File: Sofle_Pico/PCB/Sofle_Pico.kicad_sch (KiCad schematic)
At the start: 81 parts, among them J1 Pimaroni Trackball, J2 4PIN, J3 OLED, J5 Conn_01x05_Socket, J6 Conn_01x05_Socket, Q1 TIP120, SW1 SW_PUSH_LED, SW10 SW_PUSH_LED, SW11 SW_PUSH_LED, SW12 SW_PUSH_LED, SW13 SW_PUSH_LED, SW14 SW_PUSH_LED, SW15 SW_PUSH_LED, SW16 SW_PUSH_LED, SW17 SW_PUSH_LED, SW18 SW_PUSH_LED, SW19 SW_PUSH_LED, SW2 SW_PUSH_LED, SW20 SW_PUSH_LED, SW21 SW_PUSH_LED, SW22 SW_PUSH_LED, SW23 SW_PUSH_LED, SW24 SW_PUSH_LED, SW25 Rotary_Encoder_Switch, SW26 SW_PUSH_LED, SW27 SW_PUSH_LED, SW28 SW_PUSH_LED, SW29 SW_PUSH_LED, SW3 SW_PUSH_LED, SW30 SW_PUSH_LED, SW4 SW_PUSH_LED, SW5 SW_PUSH_LED, SW6 SW_PUSH_LED, SW7 SW_PUSH_LED, SW8 SW_PUSH_LED, SW9 SW_PUSH_LED, U1 SN74AHCT1G125, U3 Pico

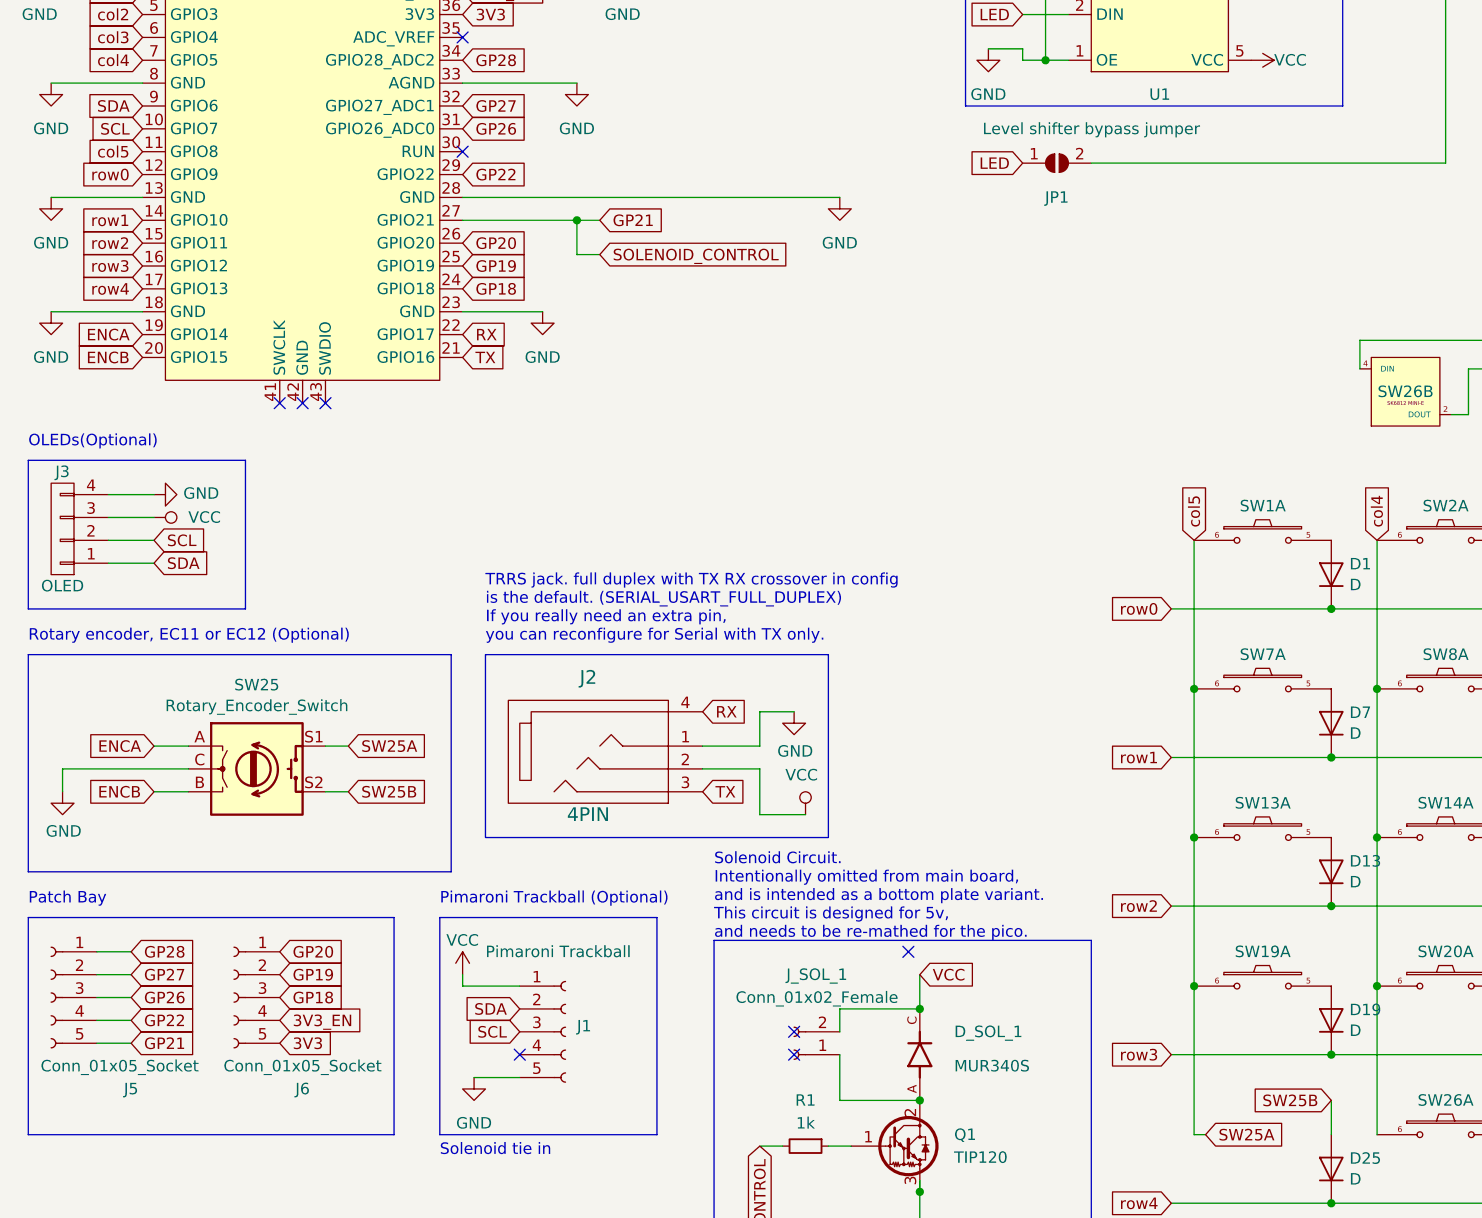
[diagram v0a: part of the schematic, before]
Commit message: Refactored LED to remove drill holes replaced drill holes with edge cuts minor trace revisions to decrease acid traps
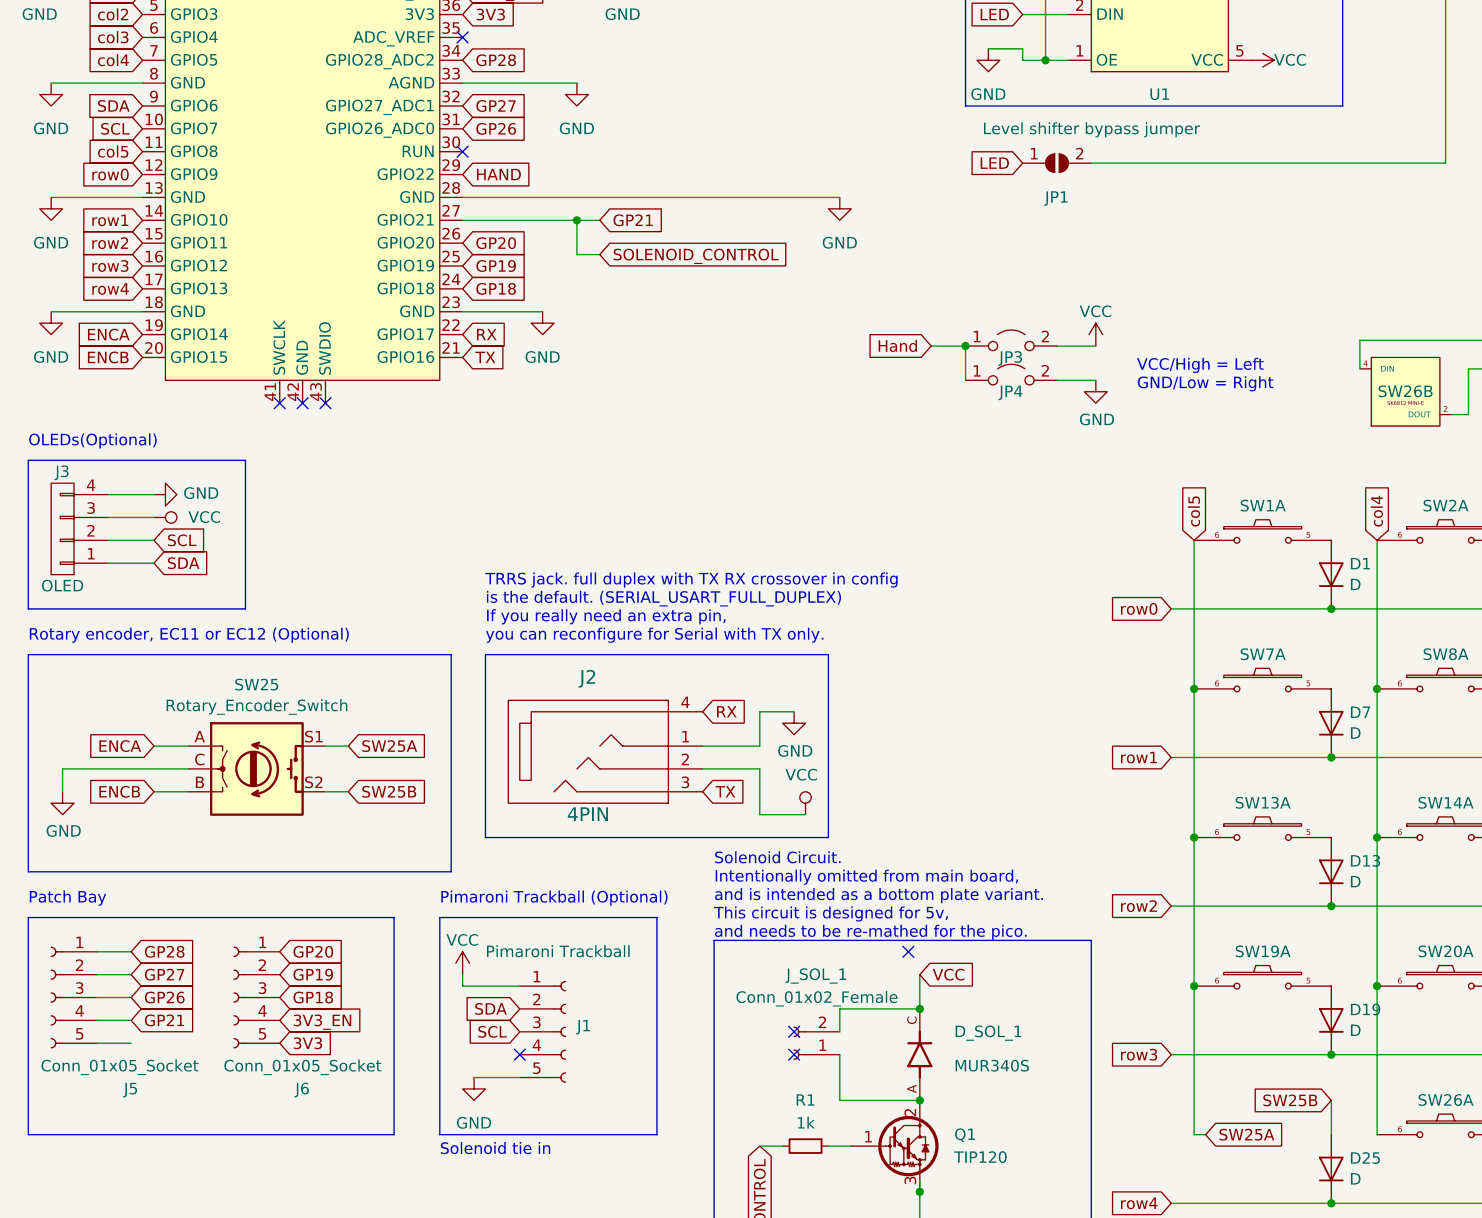
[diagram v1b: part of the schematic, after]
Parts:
- added JP3: LEFT, Keyboard Common:Jumper_Mini, symbol Jumper:Jumper_2_Open
- added JP4: RIGHT, Keyboard Common:Jumper_Mini, symbol Jumper:Jumper_2_Open
- SW1, SW10, SW11, SW12, SW13, SW14, SW15, SW16, SW17, SW18, SW19, SW2, SW20, SW21, SW22, SW23, SW24, SW26, SW27, SW28, SW29, SW3, SW30, SW4, SW5, SW6, SW7, SW8, SW9: footprint Sofle_Pico:Cherry_MX_DS_Hotswap_miniE_1U_v3.5 -> Sofle_Pico:Cherry_MX_DS_Hotswap_miniE_1U_v3.5.2
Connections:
- net GND: now also JP4.2 (B)
- net GP21: now also J5.4 (Pin_4); no longer J5.5 (Pin_5)
- net VCC: now also JP3.2 (B)
- net GP22 renamed HAND
- net HAND: no longer J5.4 (Pin_4)
- new net Hand: JP3.1 (A), JP4.1 (A)
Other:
- note added: "VCC/High = Left GND/Low = Right"

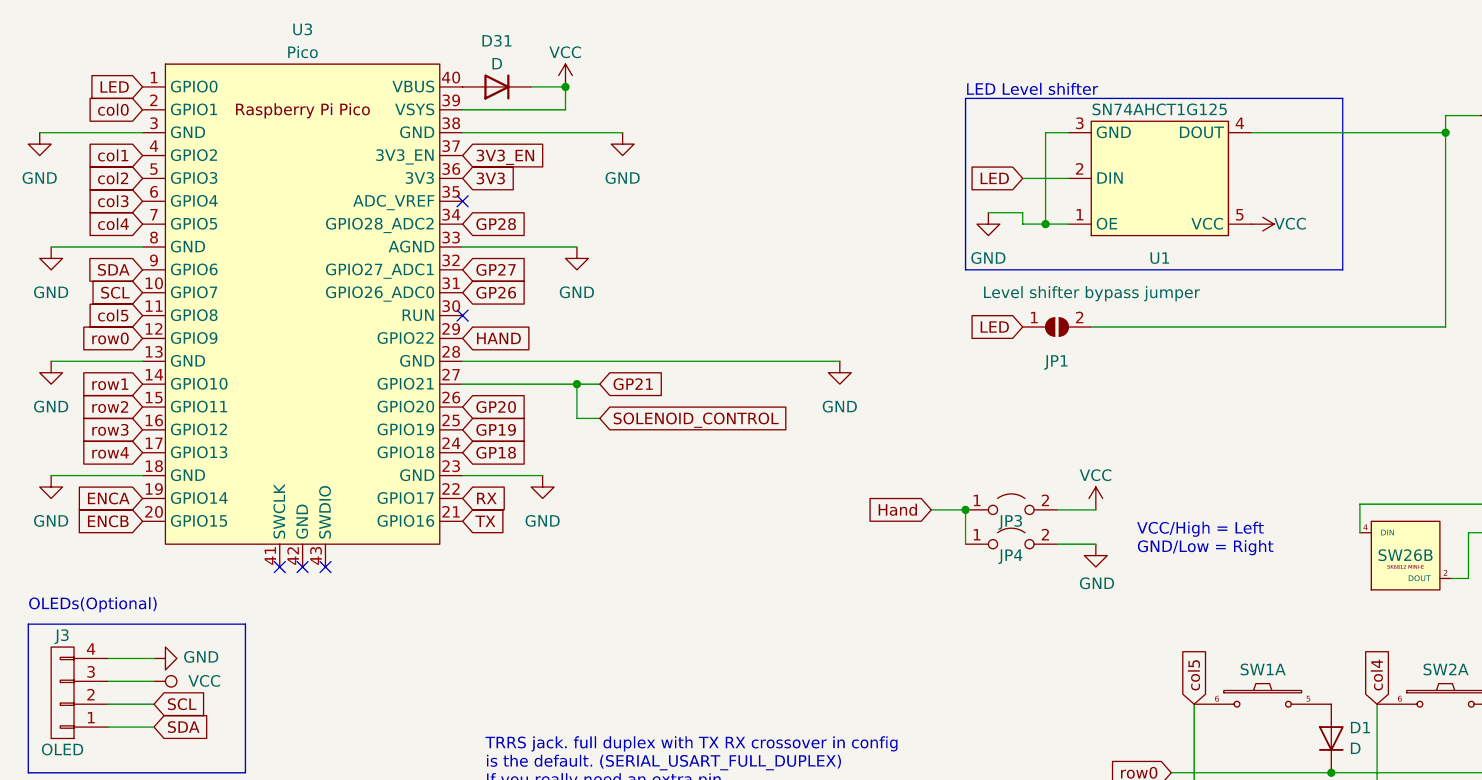
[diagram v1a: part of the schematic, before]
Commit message: Added handedness pin
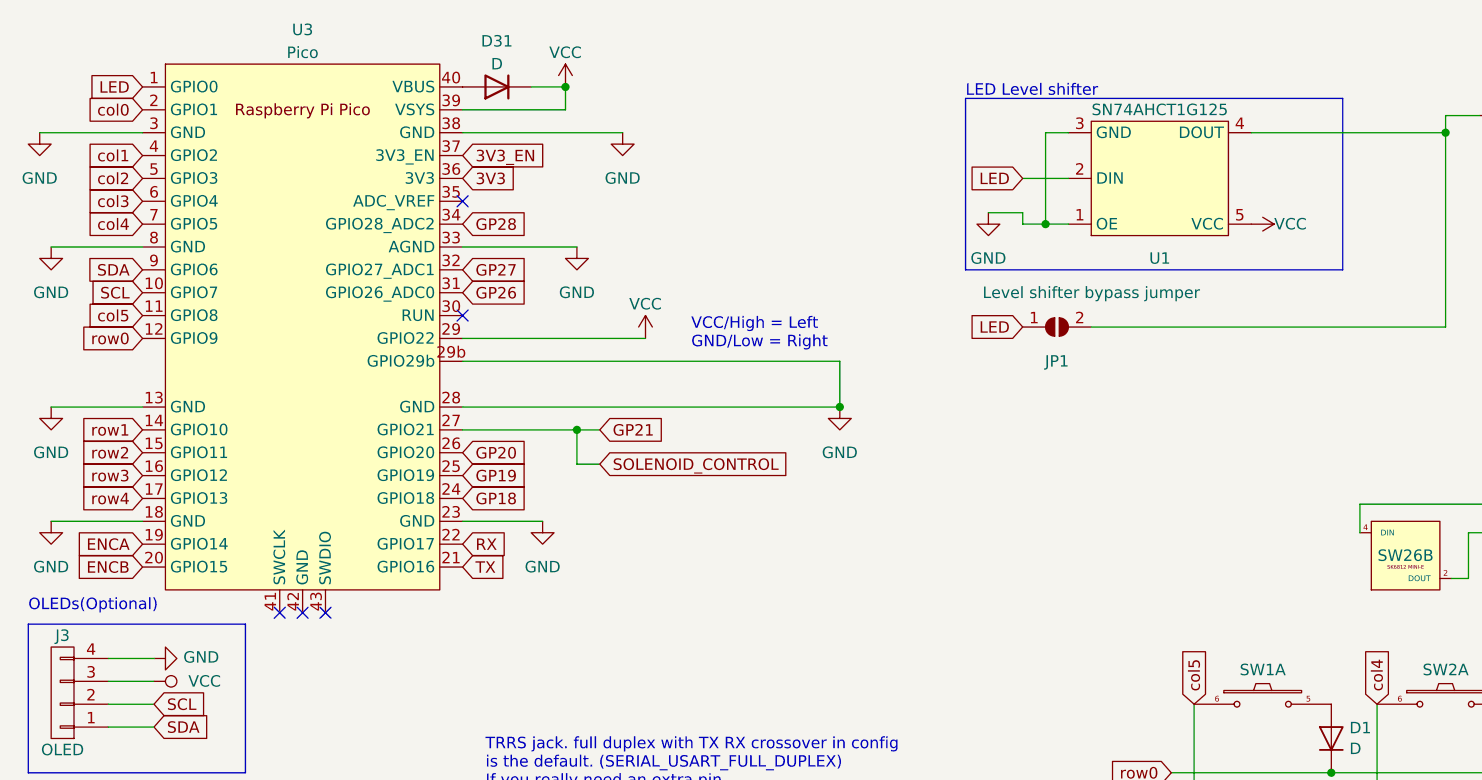
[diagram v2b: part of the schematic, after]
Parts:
- removed JP3: LEFT, Keyboard Common:Jumper_Mini, symbol Jumper:Jumper_2_Open
- removed JP4: RIGHT, Keyboard Common:Jumper_Mini, symbol Jumper:Jumper_2_Open
- U3: footprint Sofle_Pico:RPi_Pico_SMD_TH - Junco -DS Sofle v3b v3 nohole -> Sofle_Pico:RPi_Pico_SMD_TH - Junco -DS Sofle Pico handpins
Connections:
- net HAND is gone; now on net VCC: U3.29 (GPIO22)
- net GND: now also U3.29b (GPIO29b)

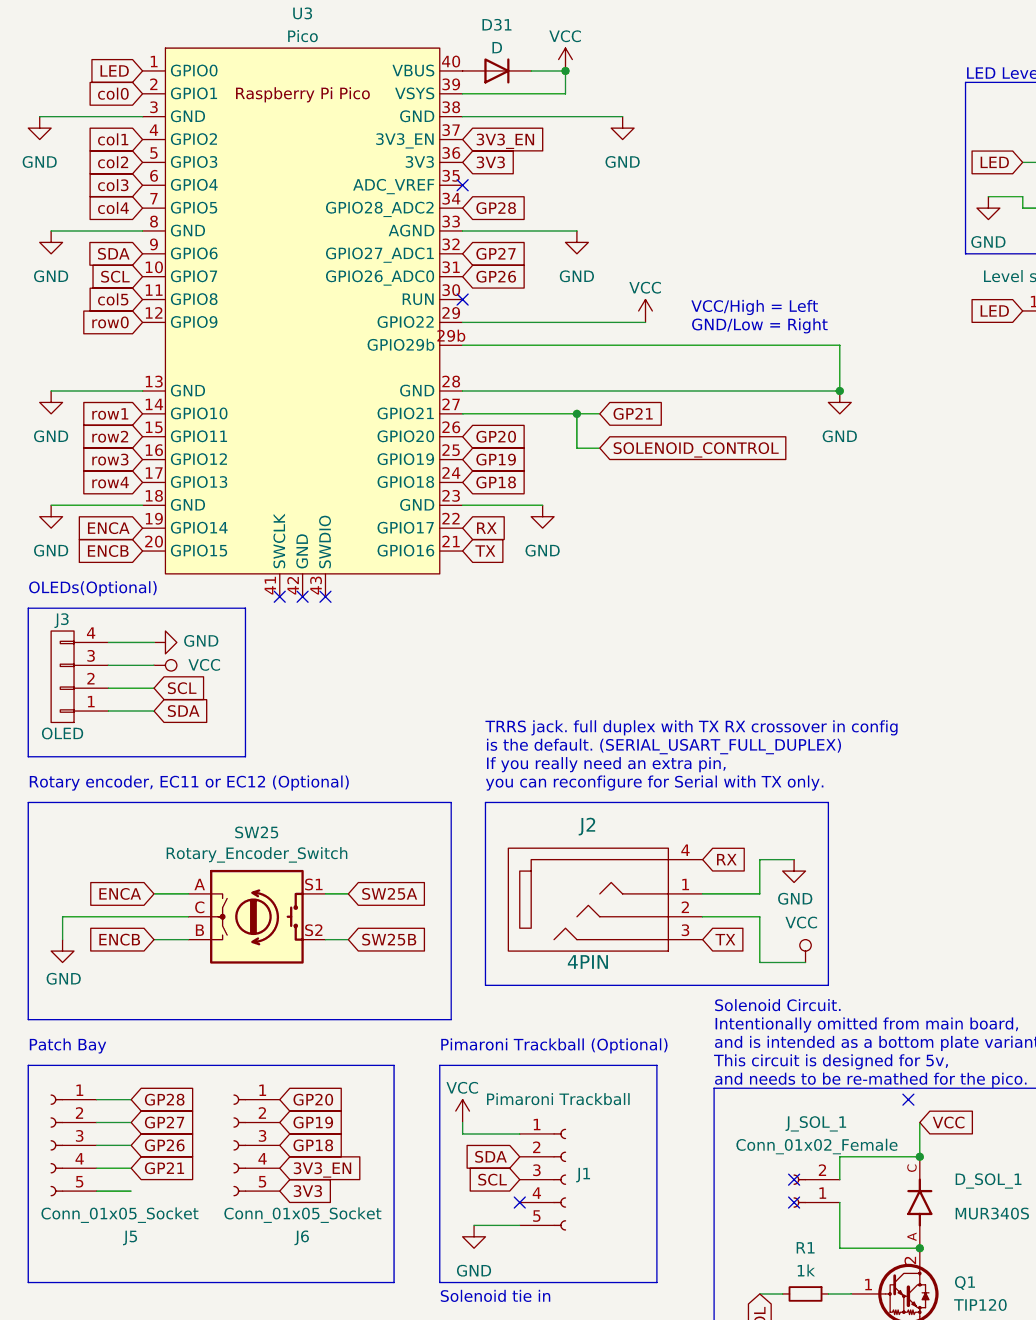
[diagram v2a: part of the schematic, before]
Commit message: Removed LED tweezer holes
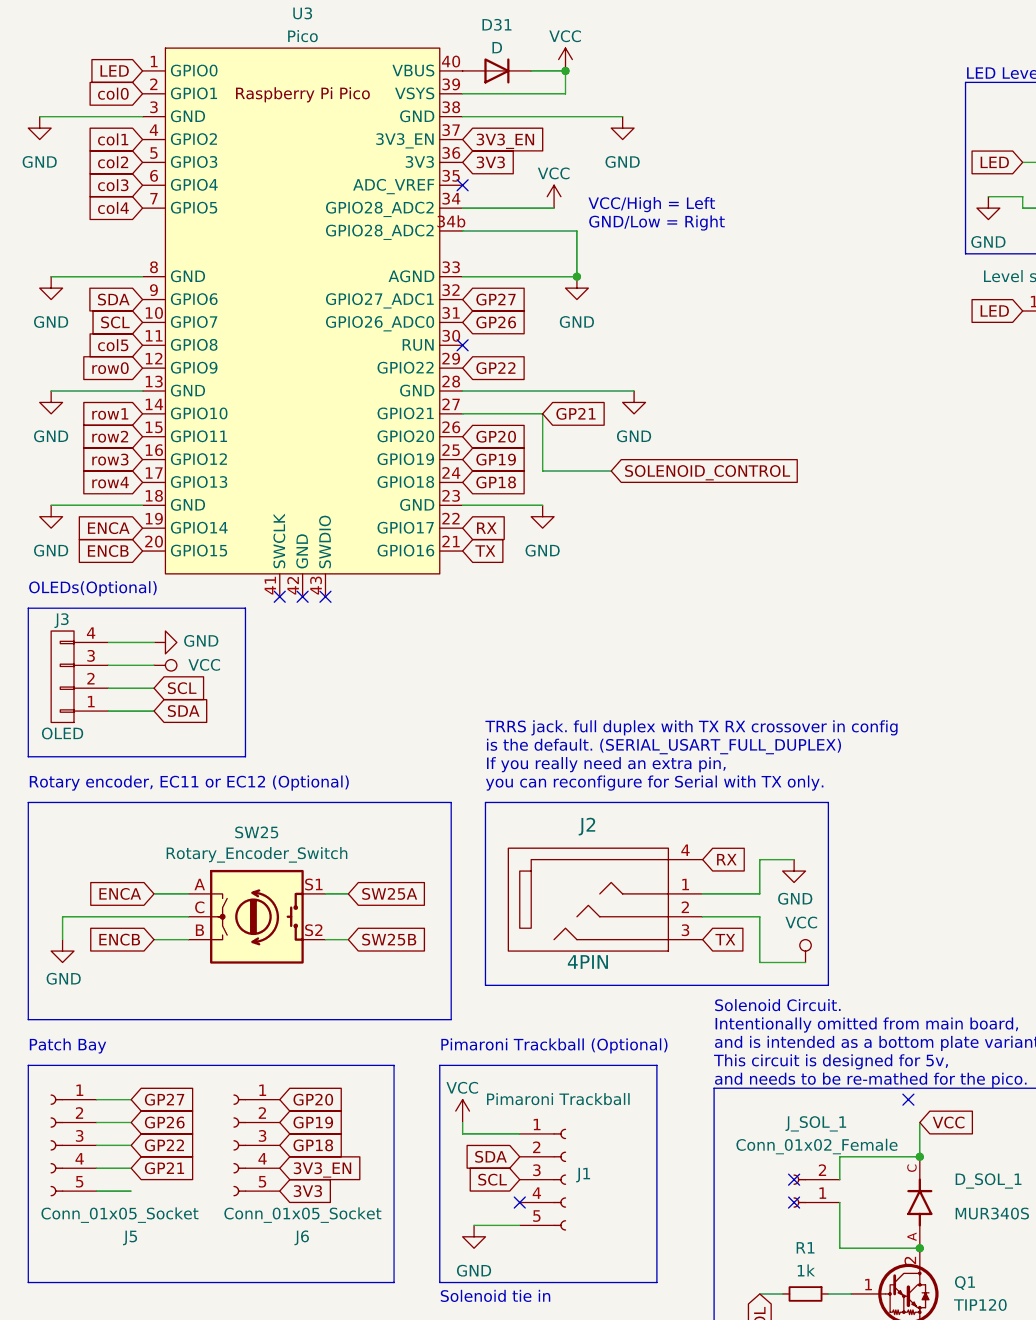
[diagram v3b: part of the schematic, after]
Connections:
- net GND: now also U3.34b (GPIO28_ADC2); no longer U3.29b (GPIO29b)
- net GP26: now also J5.2 (Pin_2); no longer J5.3 (Pin_3)
- net GP27: now also J5.1 (Pin_1); no longer J5.2 (Pin_2)
- net VCC: now also U3.34 (GPIO28_ADC2); no longer U3.29 (GPIO22)
- removed net GP28: J5.1 (Pin_1), U3.34 (GPIO28_ADC2)
- new net GP22: J5.3 (Pin_3), U3.29 (GPIO22)
